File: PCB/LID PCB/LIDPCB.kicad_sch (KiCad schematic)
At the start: 10 parts, among them J1 POWER/I2C, U1 LTR-329ALS-01, U2 LSM6DSMTR

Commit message: Main pcb reviewed
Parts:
- gave numbers to parts that had none: 2
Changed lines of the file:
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@@
   (symbol (lib_id "Mechanical:MountingHole") (at 35.56 135.89 0) (unit 1)
     (in_bom yes) (on_board yes) (fields_autoplaced)
-    (property "Reference" "H?" (id 0) (at 38.1 134.6199 0)
+    (property "Reference" "H1" (id 0) (at 38.1 134.6199 0)
       (effects (font (size 1.27 1.27)) (justify left))
     )
@@
   (symbol (lib_id "Mechanical:MountingHole") (at 35.56 142.24 0) (unit 1)
     (in_bom yes) (on_board yes) (fields_autoplaced)
-    (property "Reference" "H?" (id 0) (at 38.1 140.9699 0)
+    (property "Reference" "H2" (id 0) (at 38.1 140.9699 0)
       (effects (font (size 1.27 1.27)) (justify left))
     )
@@
     )
     (path "/65218424-0549-4444-b651-105a87047675"
-      (reference "H?") (unit 1) (value "MountingHole") (footprint "MountingHole:MountingHole_3.2mm_M3_DIN965_Pad")
+      (reference "H1") (unit 1) (value "MountingHole") (footprint "MountingHole:MountingHole_3.2mm_M3_DIN965_Pad")
     )
     (path "/dd10eb3e-603e-44ab-989e-52aaab9de688"
-      (reference "H?") (unit 1) (value "MountingHole") (footprint "MountingHole:MountingHole_3.2mm_M3_DIN965_Pad")
+      (reference "H2") (unit 1) (value "MountingHole") (footprint "MountingHole:MountingHole_3.2mm_M3_DIN965_Pad")
     )
     (path "/669b1a91-75ea-498d-98dd-913db90c9efb"

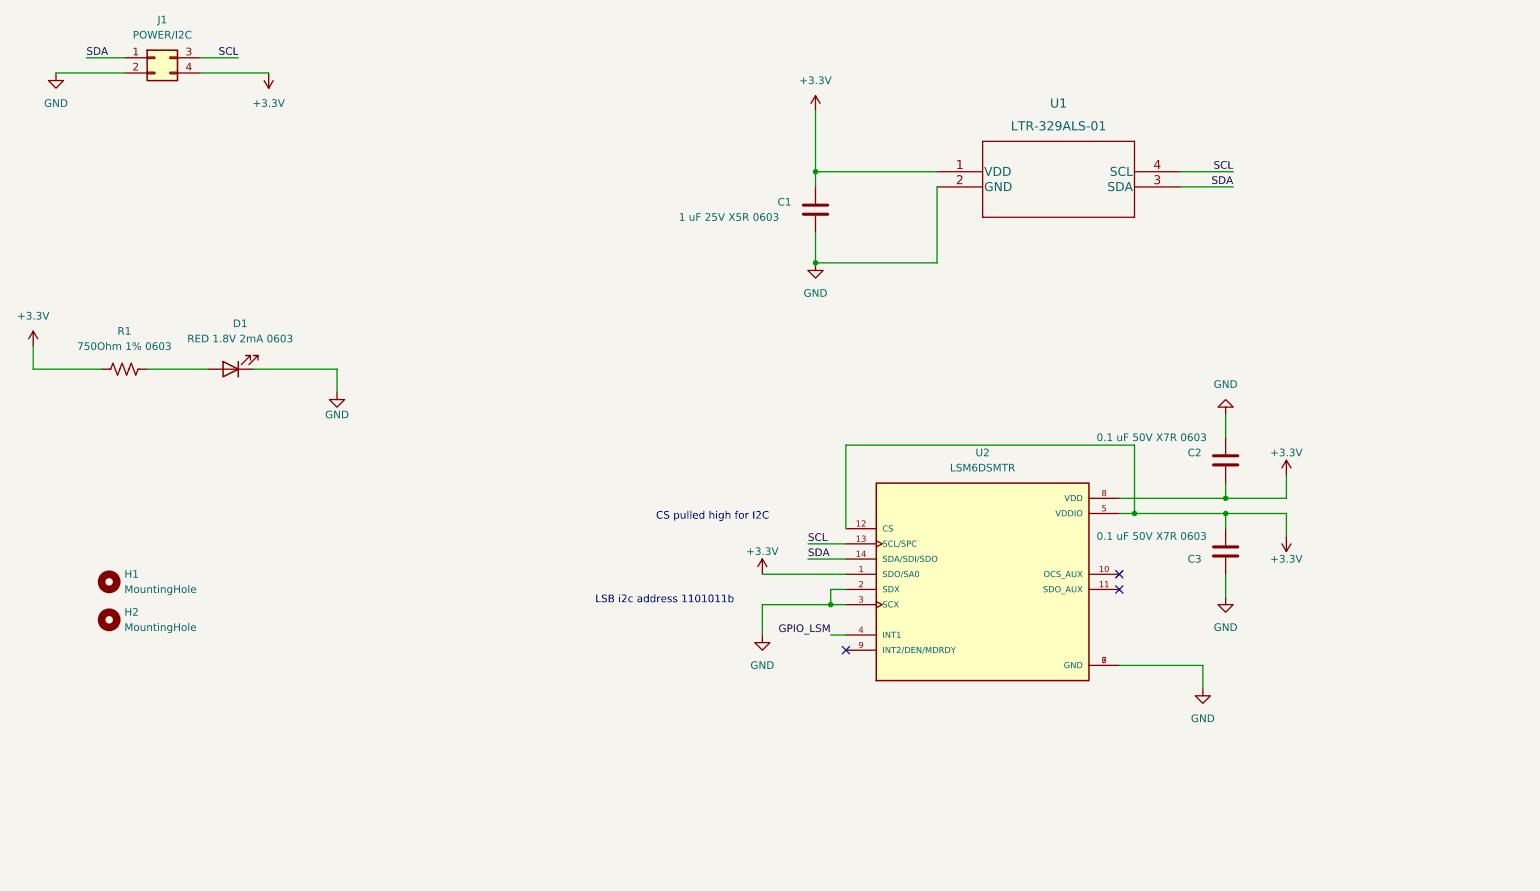
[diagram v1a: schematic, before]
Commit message: 3x PCB ready for gerberization
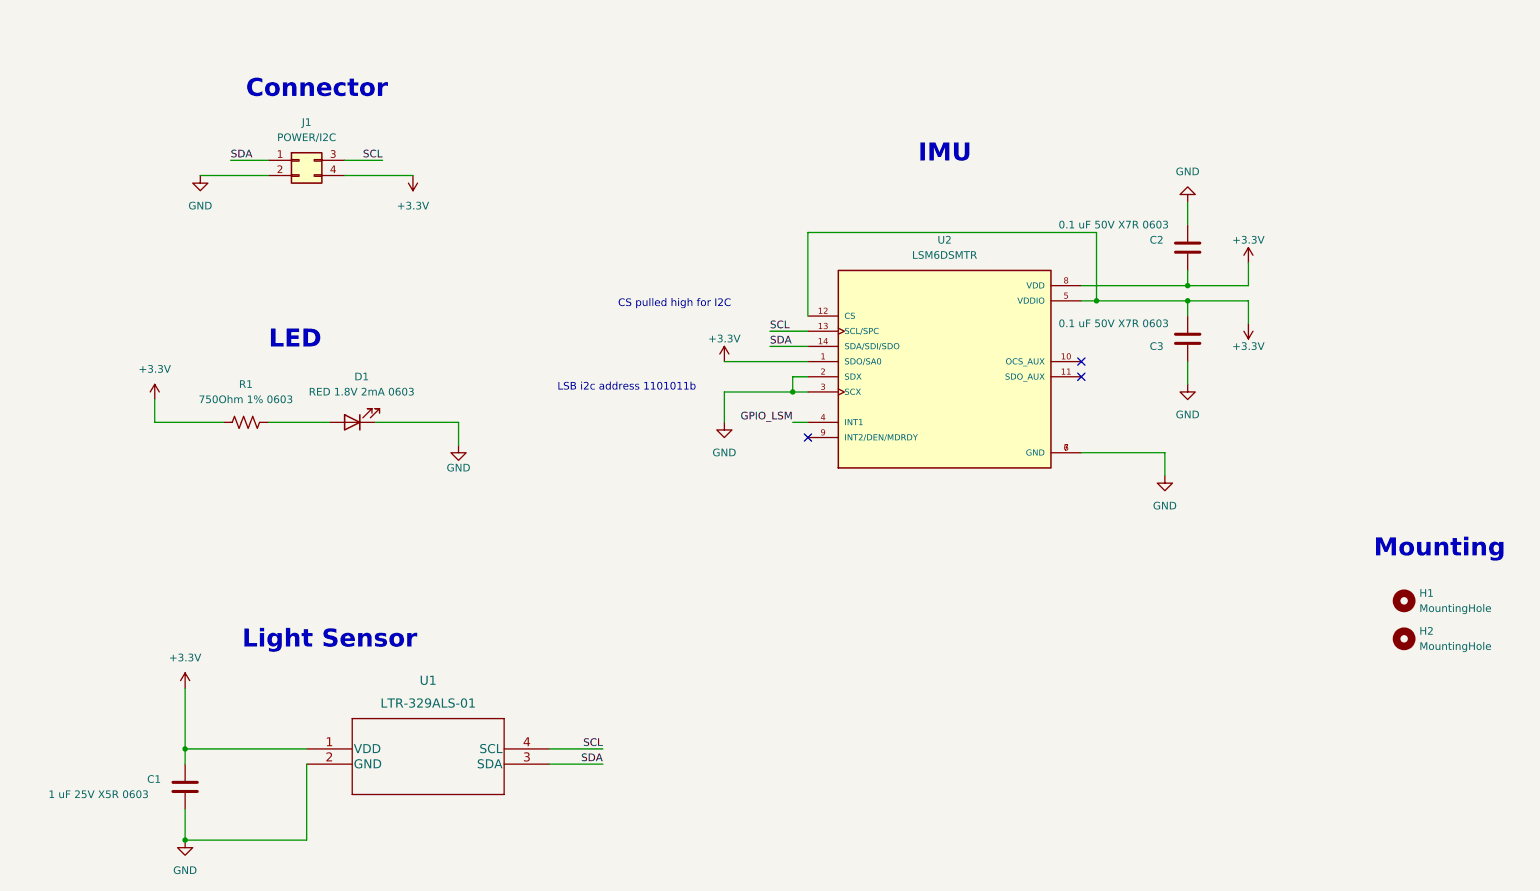
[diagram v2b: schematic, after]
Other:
- note added: "Connector"
- note added: "IMU"
- note added: "LED"
- note added: "Light Sensor"
- note added: "Mounting"
- moved on the sheet: C1, C2, C3, D1, H1, H2, J1, R1, U1, U2
